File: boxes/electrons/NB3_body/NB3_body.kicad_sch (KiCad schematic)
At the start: 38 parts, among them J1 Conn_02x05_Counter_Clockwise, J10 Conn_02x03_Top_Bottom, J11 Conn_02x03_Top_Bottom, J12 Conn_02x03_Top_Bottom, J13 JST ZH 6-way Socket, J14 JST ZH 6-way Socket, J15 Conn_02x03_Top_Bottom, J16 Conn_02x03_Top_Bottom, J2 Conn_02x05_Counter_Clockwise, J3 Conn_02x05_Counter_Clockwise, J4 Conn_02x05_Counter_Clockwise, J5 Conn_02x05_Counter_Clockwise, J6 Conn_02x05_Counter_Clockwise, J7 Conn_02x05_Counter_Clockwise, J8 Conn_02x05_Counter_Clockwise, J9 JST SH 4-way Socket

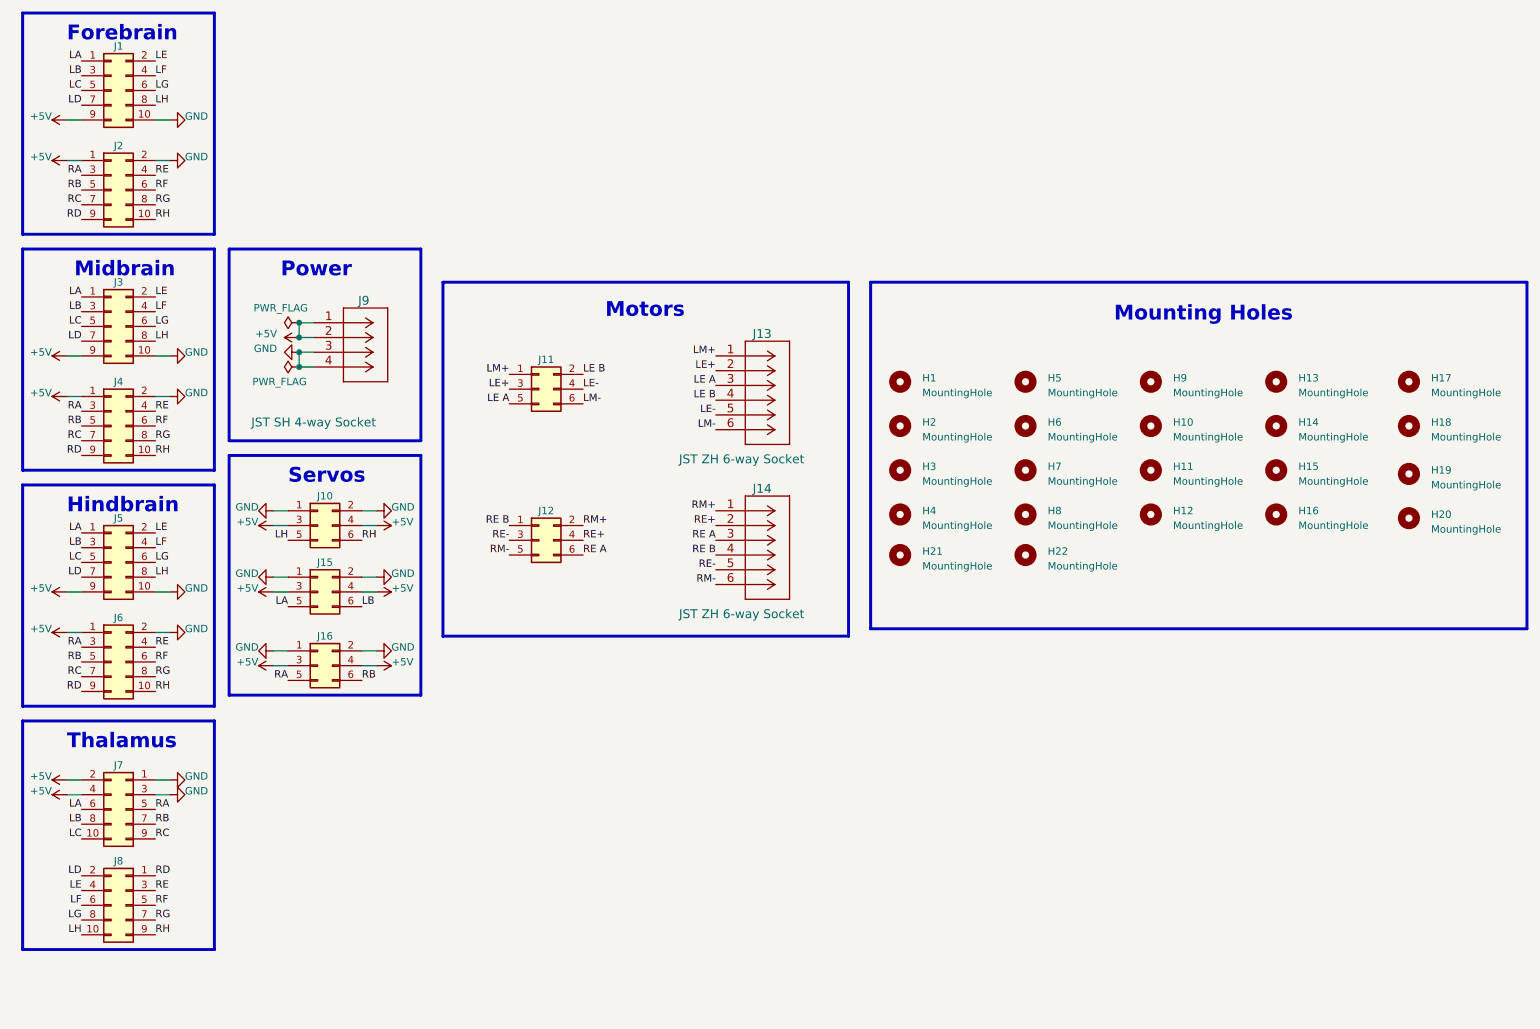
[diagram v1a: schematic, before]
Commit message: Ref 1 of NB3 Mouth
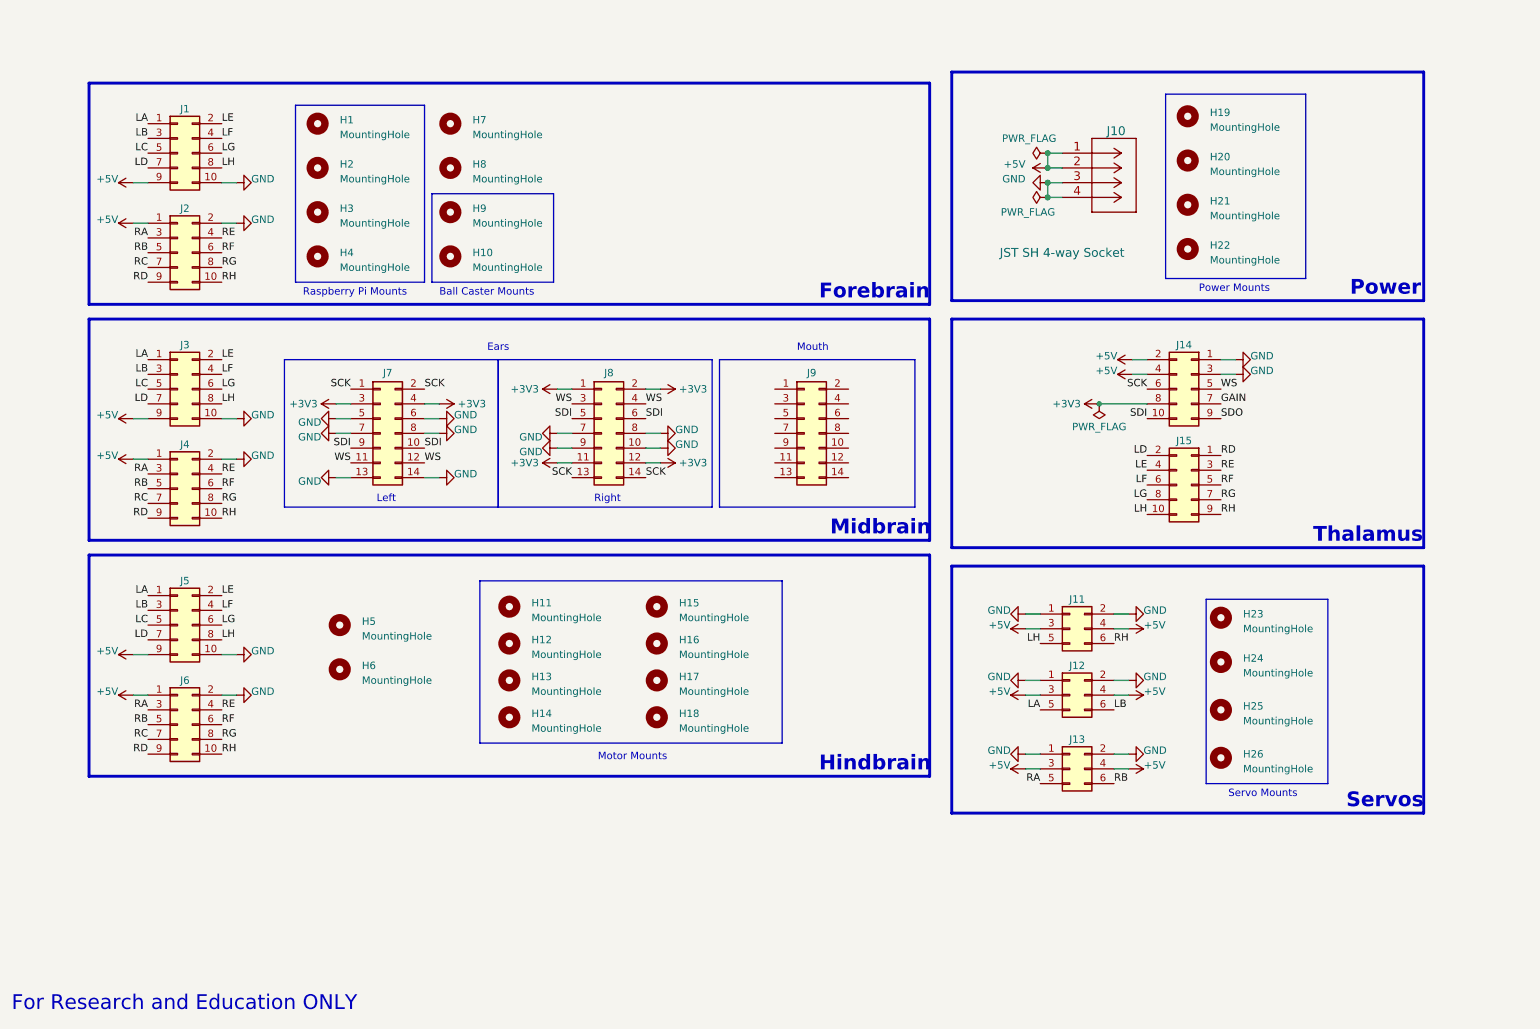
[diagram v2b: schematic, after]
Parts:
- removed H19, H20: MountingHole, MountingHole:MountingHole_2.7mm_M2.5_ISO7380_Pad, symbol Mechanical:MountingHole
- removed J11, J12: Conn_02x03_Top_Bottom, Connector_PinHeader_2.54mm:PinHeader_2x03_P2.54mm_Vertical_SMD, symbol Connector_Generic:Conn_02x03_Odd_Even
- removed J13, J14: JST ZH 6-way Socket, NB3_body:Connector_B6B-ZR-SM4-GW-TF(LF)(SN), symbol NB3_body:Connector_B6B-ZR-SM4-GW-TF(LF)(SN)
- added H13, H14, H15, H16, H17, H18: MountingHole, MountingHole:MountingHole_3.2mm_M3_ISO7380_Pad, symbol Mechanical:MountingHole
- added J7, J8, J9: Conn_02x07_Odd_Even, Connector_PinSocket_2.54mm:PinSocket_2x07_P2.54mm_Vertical_SMD, symbol Connector_Generic:Conn_02x07_Odd_Even
- H11, H12: footprint MountingHole:MountingHole_2.5mm_Pad -> MountingHole:MountingHole_3.2mm_M3_ISO7380_Pad
- H23: renamed from H9; footprint MountingHole:MountingHole_2.5mm_Pad -> MountingHole:MountingHole_2.7mm_M2.5_ISO7380_Pad
- H24: renamed from H10; footprint MountingHole:MountingHole_2.5mm_Pad -> MountingHole:MountingHole_2.7mm_M2.5_ISO7380_Pad
- H25: renamed from H21; footprint MountingHole:MountingHole_2.5mm_Pad -> MountingHole:MountingHole_2.7mm_M2.5_ISO7380_Pad
- H26: renamed from H22; footprint MountingHole:MountingHole_2.5mm_Pad -> MountingHole:MountingHole_2.7mm_M2.5_ISO7380_Pad
- renumbered H5 to H1, H18 to H10, H1 to H19, H6 to H2, H2 to H20, H3 to H21, H4 to H22, H7 to H3, H8 to H4, H15 to H5, H16 to H6, H13 to H7, H14 to H8, H17 to H9, J9 to J10, J10 to J11, J15 to J12, J16 to J13, J7 to J14, J8 to J15
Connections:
- net GND: now also J7.13 (Pin_13), J7.14 (Pin_14), J7.5 (Pin_5), J7.6 (Pin_6), J7.7 (Pin_7), J7.8 (Pin_8), J8.10 (Pin_10), J8.7 (Pin_7), J8.8 (Pin_8), J8.9 (Pin_9)
- net LA: no longer J14.6 (Pin_6)
- net LB: no longer J14.8 (Pin_8)
- net LC: no longer J14.10 (Pin_10)
- net RA: no longer J14.5 (Pin_5)
- net RB: no longer J14.7 (Pin_7)
- net RC: no longer J14.9 (Pin_9)
- new net +3V3: J14.8 (Pin_8), J7.3 (Pin_3), J7.4 (Pin_4), J8.1 (Pin_1), J8.11 (Pin_11), J8.12 (Pin_12), J8.2 (Pin_2)
- new net GAIN: J14.7 (Pin_7)
- new net SCK: J14.6 (Pin_6), J7.1 (Pin_1), J7.2 (Pin_2), J8.13 (Pin_13), J8.14 (Pin_14)
- new net SDI: J14.10 (Pin_10), J7.10 (Pin_10), J7.9 (Pin_9), J8.5 (Pin_5), J8.6 (Pin_6)
- new net SDO: J14.9 (Pin_9)
- new net WS: J14.5 (Pin_5), J7.11 (Pin_11), J7.12 (Pin_12), J8.3 (Pin_3), J8.4 (Pin_4)
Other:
- note added: "Ball Caster Mounts"
- note added: "Ears"
- note added: "For Research and Education ONLY"
- note added: "Left"
- note added: "Motor Mounts"
- note added: "Mouth"
- note added: "Power Mounts"
- note added: "Raspberry Pi Mounts"
- note added: "Right"
- note added: "Servo Mounts"
- note removed: "Motors"
- note removed: "Mounting Holes"
- moved on the sheet: H1, H10, H19, H2, H20, H21, H22, H23, H24, H25, H26, H3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

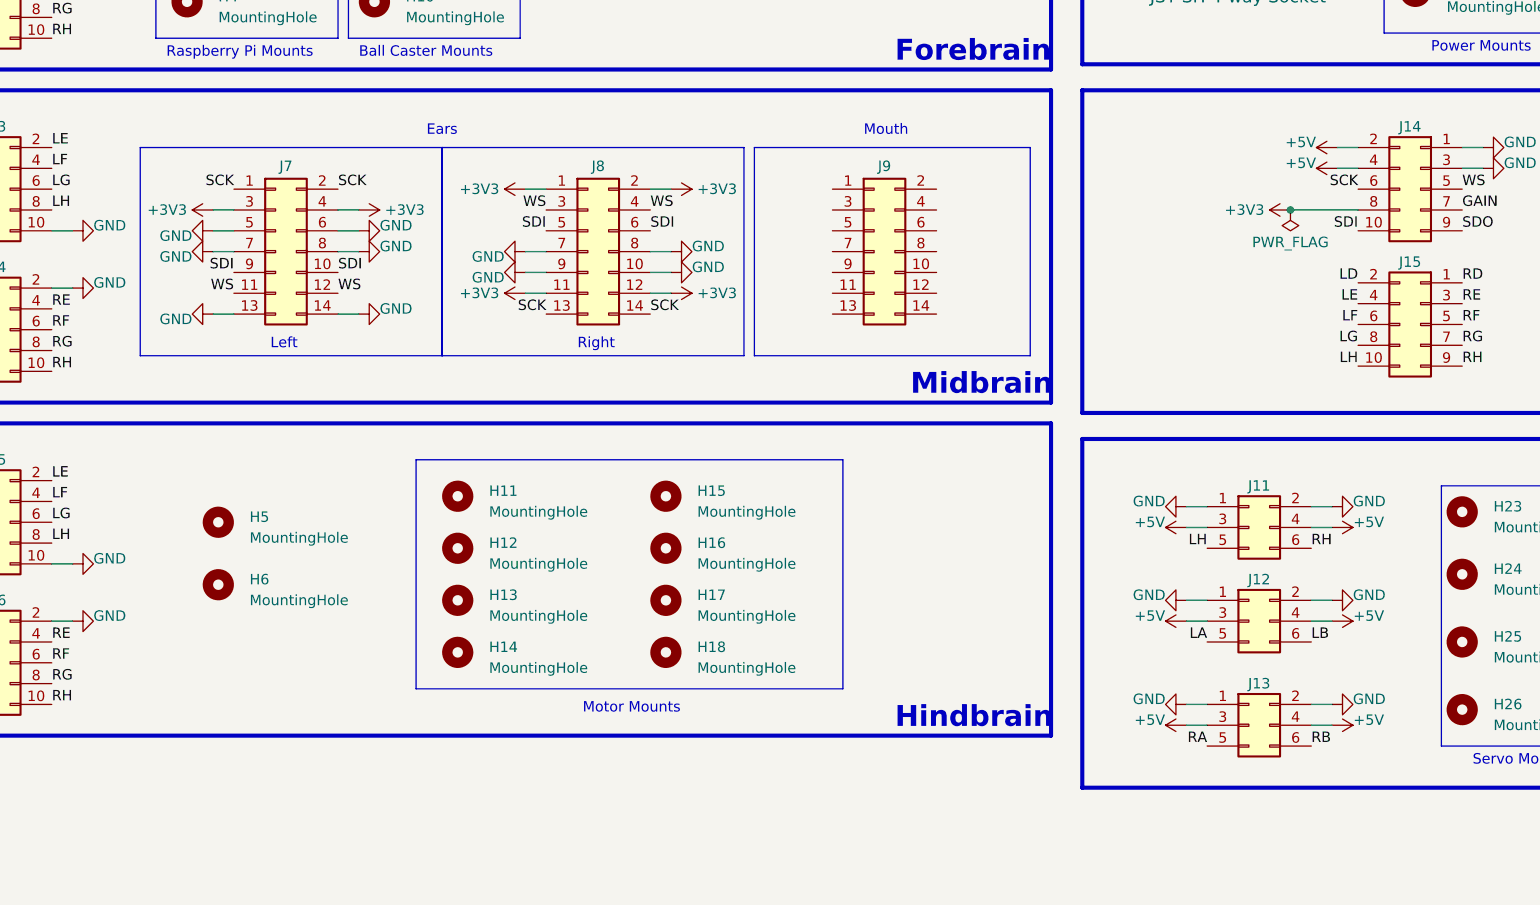
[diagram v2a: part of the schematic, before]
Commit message: Work on NB3_bidy (v4) - TT DC motors
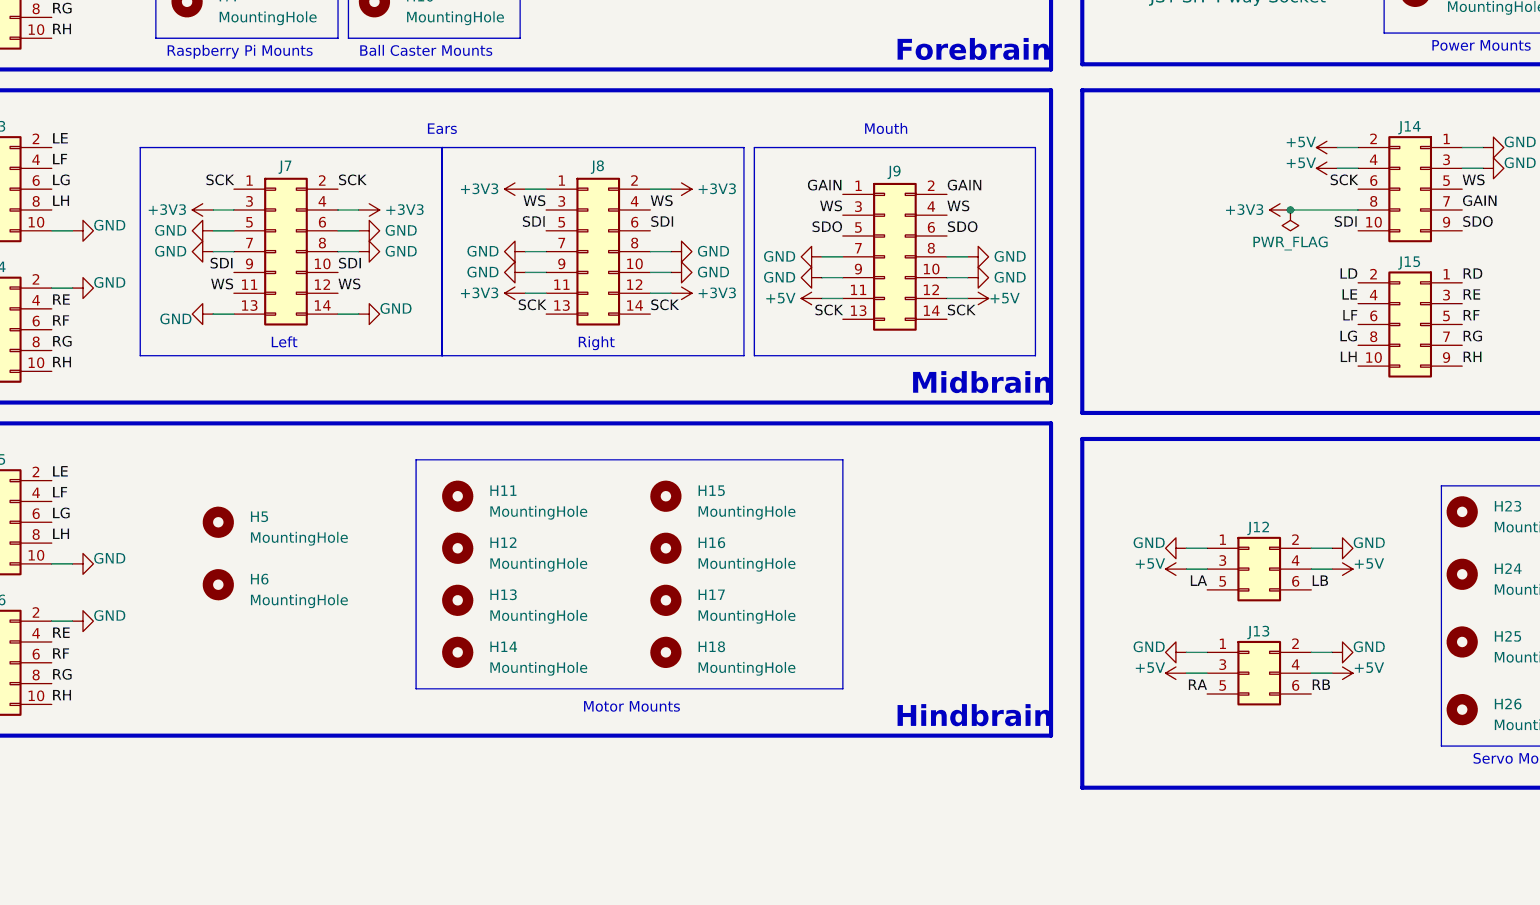
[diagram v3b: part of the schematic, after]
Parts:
- removed J11: Conn_02x03_Top_Bottom, Connector_PinHeader_2.54mm:PinHeader_2x03_P2.54mm_Vertical_SMD, symbol Connector_Generic:Conn_02x03_Odd_Even
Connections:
- net +5V: now also J9.11 (Pin_11), J9.12 (Pin_12)
- net GAIN: now also J9.1 (Pin_1), J9.2 (Pin_2)
- net GND: now also J9.10 (Pin_10), J9.7 (Pin_7), J9.8 (Pin_8), J9.9 (Pin_9)
- net SCK: now also J9.13 (Pin_13), J9.14 (Pin_14)
- net SDO: now also J9.5 (Pin_5), J9.6 (Pin_6)
- net WS: now also J9.3 (Pin_3), J9.4 (Pin_4)
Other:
- moved on the sheet: J12, J13, J9
